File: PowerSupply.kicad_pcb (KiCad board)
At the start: 2 copper layers, 22 x 12.5 mm, 10 parts, among them P1 USB_OTG, P2 CONN_01X03, U1 LM3671MF-3.3

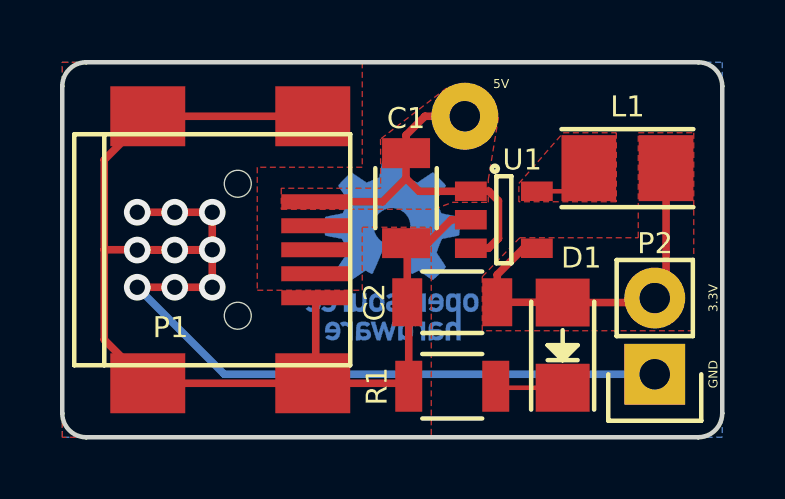
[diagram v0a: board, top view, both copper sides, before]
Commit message: Adds "POWER" label to F.Mask
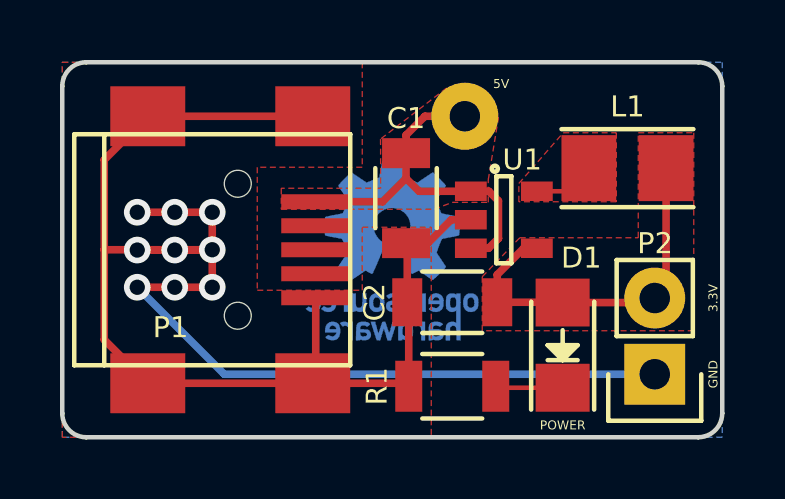
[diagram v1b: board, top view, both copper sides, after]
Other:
- board text added: "POWER"
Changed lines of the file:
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@@
     (area 49.924999 149.924999 72.075001 162.575001)
     (thickness 1.6)
-    (drawings 12)
+    (drawings 13)
     (tracks 65)
     (zones 0)
@@
       (xy 0.376964 2.709982)) (layer B.Cu) (width 0.01))
   )
+  (gr_text POWER (at 66.68 162.1) (layer F.SilkS)
+    (effects (font (size 0.3 0.3) (thickness 0.05)))
+  )
   (gr_text GND (at 71.7 160.4 90) (layer F.SilkS)

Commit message: Bumped version to v1.5 Final updates to pcb for production Updated version label (v1.5) Increased solder mask clearance to 3 mils Updated solid copper area around 5V test pin Added .gitignore file (*-bak, backup files)
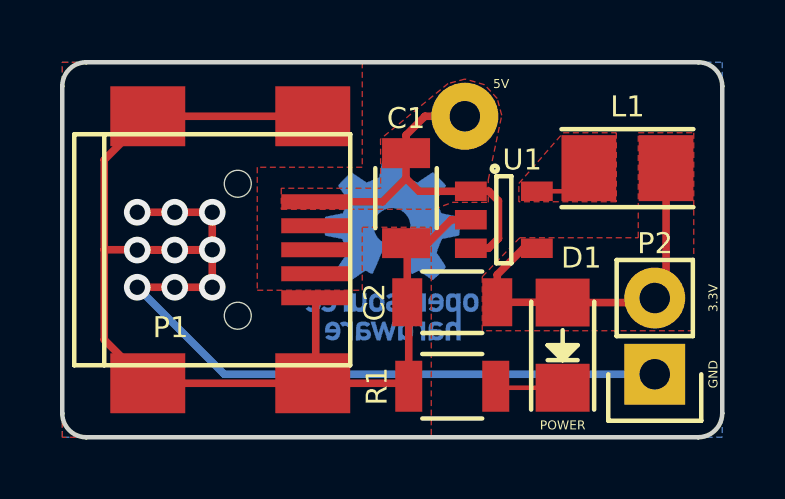
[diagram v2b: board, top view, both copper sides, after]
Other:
- rule pad_to_mask_clearance: 0.0508 -> 0.0762
- board text added: "LM3671 v1.5"
- board text removed: "LM3671 v1.3"
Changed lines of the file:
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@@
     (pad_size 2.2352 2.2352)
     (pad_drill 1.016)
-    (pad_to_mask_clearance 0.0508)
+    (pad_to_mask_clearance 0.0762)
     (aux_axis_origin 155.36 152.58)
     (grid_origin 155.23 152.45)
@@
     )
   )
-  (module Connect:USB_Mini-B locked (layer F.Cu)
+  (module Connect:USB_Mini-B (layer F.Cu)
     (at 55 156.25)
     (descr "USB Mini-B 5-pin SMD connector")
@@
     (effects (font (size 1.5 1.5) (thickness 0.2)) (justify mirror))
   )
-  (gr_text "LM3671 v1.3\n" (at 55.88 151.57) (layer B.SilkS)
+  (gr_text "LM3671 v1.5" (at 55.88 151.57) (layer B.SilkS)
     (effects (font (size 1 1) (thickness 0.1)) (justify mirror))
   )
@@
       (pts
         (xy 57.3 154.9) (xy 62.4 154.9) (xy 63 154.67) (xy 64.2 154.67) (xy 64.2 153.92)
-        (xy 64.54 151.85) (xy 62.81 150.86) (xy 60.61 152.56) (xy 60.615 154.2) (xy 57.3 154.2)
+        (xy 64.65 151.77) (xy 64.5 151.21) (xy 64.08 150.75) (xy 63.43 150.56) (xy 62.86 150.71)
+        (xy 60.61 152.56) (xy 60.615 154.2) (xy 57.3 154.2)
       )
     )

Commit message: Adds thermal relief to ground pin in P2 connector Bumped version 1.6, regenerated gerber files
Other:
- board text added: "LM3671 v1.6"
- board text removed: "LM3671 v1.5"
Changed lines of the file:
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@@
-(kicad_pcb (version 4) (host pcbnew 4.0.3-stable)
+(kicad_pcb (version 4) (host pcbnew 4.0.4-stable)
   (general
     (links 19)
@@
     (mod_text_size 1 1)
     (mod_text_width 0.15)
-    (pad_size 2.2352 2.2352)
+    (pad_size 2.032 2.032)
     (pad_drill 1.016)
     (pad_to_mask_clearance 0.0762)
@@
     (fp_line (start -1.27 3.81) (end 1.27 3.81) (layer F.SilkS) (width 0.15))
     (pad 1 thru_hole rect (at 0 0 180) (size 2.032 2.032) (drill 1.016) (layers *.Cu *.Mask F.SilkS)
-      (net 2 GND))
+      (net 2 GND) (zone_connect 1) (thermal_width 0.508) (thermal_gap 0.254))
     (pad 2 thru_hole oval (at 0 2.54 180) (size 2.032 2.032) (drill 1.016) (layers *.Cu *.Mask F.SilkS)
       (net 3 +3V3))
@@
     (effects (font (size 1.5 1.5) (thickness 0.2)) (justify mirror))
   )
-  (gr_text "LM3671 v1.5" (at 55.88 151.57) (layer B.SilkS)
+  (gr_text "LM3671 v1.6" (at 55.88 151.57) (layer B.SilkS)
     (effects (font (size 1 1) (thickness 0.1)) (justify mirror))
   )

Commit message: Updates value of C2 to 22 pF
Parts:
- C2: value 10uF -> 22uF
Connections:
- P1 pad 2: (no net) -> Net-(P1-Pad2)
- P1 pad 3: (no net) -> Net-(P1-Pad3)
- P1 pad 4: (no net) -> Net-(P1-Pad4)
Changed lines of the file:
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@@
     (zones 0)
     (modules 10)
-    (nets 6)
+    (nets 9)
   )
   (page A4)
@@
   (net 4 "Net-(L1-Pad1)")
   (net 5 "Net-(D1-Pad1)")
+  (net 6 "Net-(P1-Pad2)")
+  (net 7 "Net-(P1-Pad3)")
+  (net 8 "Net-(P1-Pad4)")
   (net_class Default "This is the default net class."
     (clearance 0.1524)
@@
     (add_net "Net-(D1-Pad1)")
     (add_net "Net-(L1-Pad1)")
+    (add_net "Net-(P1-Pad2)")
+    (add_net "Net-(P1-Pad3)")
+    (add_net "Net-(P1-Pad4)")
   )
   (net_class Power ""
@@
     (pad 1 smd rect (at 3.44932 -1.6002) (size 2.30124 0.50038) (layers F.Cu F.Paste F.Mask)
       (net 1 VCC))
-    (pad 2 smd rect (at 3.44932 -0.8001) (size 2.30124 0.50038) (layers F.Cu F.Paste F.Mask))
-    (pad 3 smd rect (at 3.44932 0) (size 2.30124 0.50038) (layers F.Cu F.Paste F.Mask))
-    (pad 4 smd rect (at 3.44932 0.8001) (size 2.30124 0.50038) (layers F.Cu F.Paste F.Mask))
+    (pad 2 smd rect (at 3.44932 -0.8001) (size 2.30124 0.50038) (layers F.Cu F.Paste F.Mask)
+      (net 6 "Net-(P1-Pad2)"))
+    (pad 3 smd rect (at 3.44932 0) (size 2.30124 0.50038) (layers F.Cu F.Paste F.Mask)
+      (net 7 "Net-(P1-Pad3)"))
+    (pad 4 smd rect (at 3.44932 0.8001) (size 2.30124 0.50038) (layers F.Cu F.Paste F.Mask)
+      (net 8 "Net-(P1-Pad4)"))
     (pad 5 smd rect (at 3.44932 1.6002) (size 2.30124 0.50038) (layers F.Cu F.Paste F.Mask)
       (net 2 GND))
@@
       (effects (font (size 0.7 0.7) (thickness 0.15)))
     )
-    (fp_text value 10uF (at 0 2.3 180) (layer F.Fab)
-      (effects (font (size 1 1) (thickness 0.15)))
-    )
+    (fp_text value 22uF (at 0 2.3 180) (layer F.Fab)
+      (effects (font (size 1 1) (thickness 0.15)))
+    )
